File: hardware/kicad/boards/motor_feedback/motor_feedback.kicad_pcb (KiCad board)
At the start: 2 copper layers, 104 x 104 mm, 10 parts, among them J1 Screw_Terminal_01x03, J3 Screw_Terminal_01x03, U10 IL300, U11 MCP601, U9 MCP601

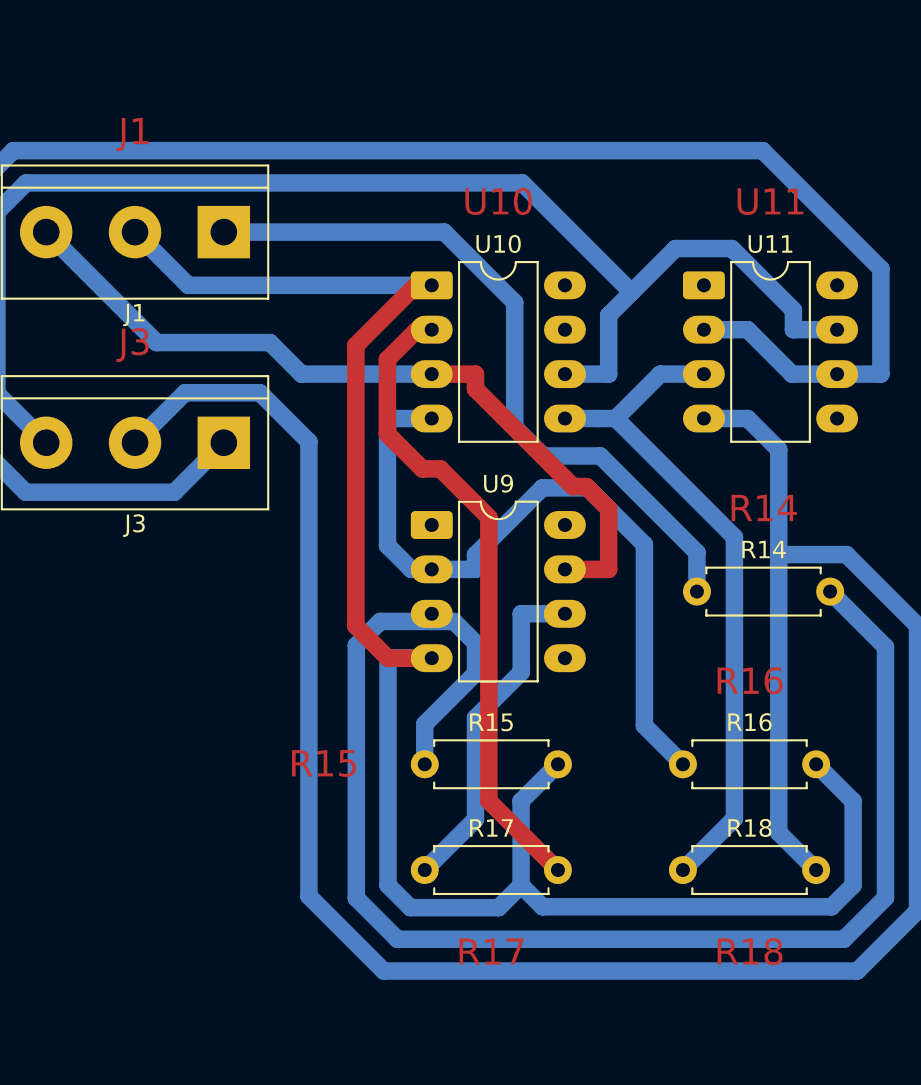
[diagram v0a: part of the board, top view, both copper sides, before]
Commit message: Refdes on silkscreen, never on top copper
Component reference designators now go on F.SilkS (top silkscreen) instead of
being etched as copper text on F.Cu. Footprint default refs are hidden so there's
one clean label per part; placement only avoids pads (silk-over-copper is fine),
so nothing drops. Also fixes the finish step's zone-removal to materialize lists
before Remove() (KiCad-10 SWIG iterators invalidate on mutation). motor_power +
motor_feedback re-finished to silk.
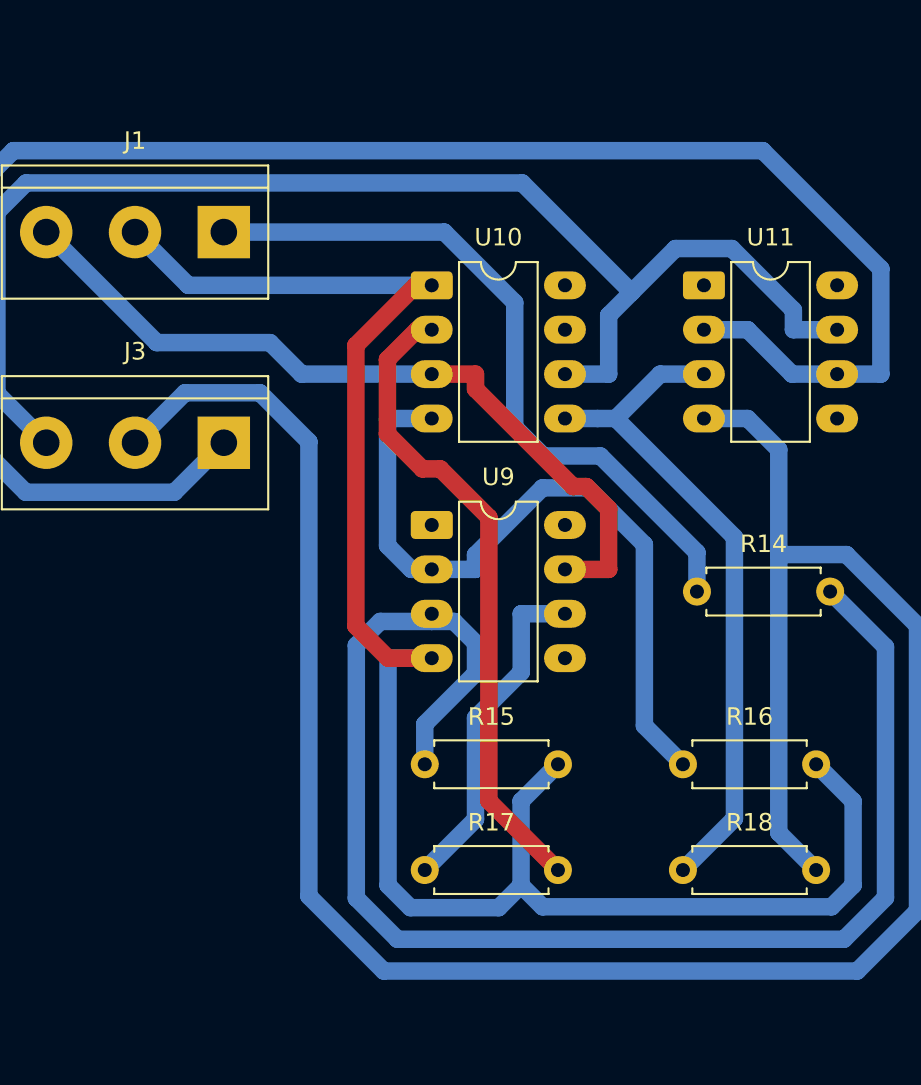
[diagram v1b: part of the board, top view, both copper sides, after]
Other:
- board text added: "U9"
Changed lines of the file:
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@@
 			(at 3.81 -2.33 0)
 			(layer "F.SilkS")
+			(hide yes)
 			(effects
 				(font
@@
 			(at 3.81 -2.33 0)
 			(layer "F.SilkS")
+			(hide yes)
 			(effects
 				(font
@@
 			(at 3.81 -2.37 0)
 			(layer "F.SilkS")
+			(hide yes)
 			(effects
 				(font
@@
 			(at 5.05 -4.65 180)
 			(layer "F.SilkS")
+			(hide yes)
 			(effects
 				(font
@@
 			(at 3.81 -2.37 0)
 			(layer "F.SilkS")
+			(hide yes)
 			(effects
 				(font
@@
 			(at 3.81 -2.37 0)
 			(layer "F.SilkS")
+			(hide yes)
 			(effects
 				(font
@@
 			(at 5.05 -4.65 180)
 			(layer "F.SilkS")
+			(hide yes)
 			(effects
 				(font
@@
 			(at 3.81 -2.33 0)
 			(layer "F.SilkS")
+			(hide yes)
 			(effects
 				(font
@@
 			(at 3.81 -2.37 0)
 			(layer "F.SilkS")
+			(hide yes)
 			(effects
 				(font
@@
 			(at 3.81 -2.37 0)
 			(layer "F.SilkS")
+			(hide yes)
 			(effects
 				(font
@@
 	)
 	(gr_text "J1"
-		(at 55.0925 49.2775 0)
-		(layer "F.Cu")
+		(at 55.0925 49.7775 0)
+		(layer "F.SilkS")
 		(effects
 			(font
-				(size 1.5 1.5)
-				(thickness 0.3)
+				(size 1 1)
+				(thickness 0.15)
 			)
 		)
 	)
 	(gr_text "J3"
-		(at 55.0925 61.3275 0)
-		(layer "F.Cu")
+		(at 55.0925 61.8275 0)
+		(layer "F.SilkS")
 		(effects
 			(font
-				(size 1.5 1.5)
-				(thickness 0.3)
+				(size 1 1)
+				(thickness 0.15)
 			)
 		)
 	)
 	(gr_text "R15"
-		(at 65.8925 85.4475 0)
-		(layer "F.Cu")
+		(at 75.4775 82.7225 0)
+		(layer "F.SilkS")
 		(effects
 			(font
-				(size 1.5 1.5)
-				(thickness 0.3)
+				(size 1 1)
+				(thickness 0.15)
 			)
 		)
 	)
 	(gr_text "R17"
-		(at 75.4775 96.2225 0)
-		(layer "F.Cu")
+		(at 75.4775 88.7725 0)
+		(layer "F.SilkS")
 		(effects
 			(font
-				(size 1.5 1.5)
-				(thickness 0.3)
+				(size 1 1)
+				(thickness 0.15)
 			)
 		)
 	)
 	(gr_text "U10"
-		(at 75.8775 53.3025 0)
-		(layer "F.Cu")
+		(at 75.8775 55.3025 0)
+		(layer "F.SilkS")
 		(effects
 			(font
-				(size 1.5 1.5)
-				(thickness 0.3)
+				(size 1 1)
+				(thickness 0.15)
+			)
+		)
+	)
+	(gr_text "U9"
+		(at 75.8775 69.0125 0)
+		(layer "F.SilkS")
+		(effects
+			(font
+				(size 1 1)
+				(thickness 0.15)
 			)
 		)
 	)
 	(gr_text "R16"
-		(at 90.2475 80.7225 0)
-		(layer "F.Cu")
+		(at 90.2475 82.7225 0)
+		(layer "F.SilkS")
 		(effects
 			(font
-				(size 1.5 1.5)
-				(thickness 0.3)
+				(size 1 1)
+				(thickness 0.15)
 			)
 		)
 	)
 	(gr_text "R18"
-		(at 90.2475 96.2225 0)
-		(layer "F.Cu")
+		(at 90.2475 88.7725 0)
+		(layer "F.SilkS")
 		(effects
 			(font
-				(size 1.5 1.5)
-				(thickness 0.3)
+				(size 1 1)
+				(thickness 0.15)
 			)
 		)
 	)
 	(gr_text "R14"
-		(at 91.0475 70.8425 0)
-		(layer "F.Cu")
+		(at 91.0475 72.8425 0)
+		(layer "F.SilkS")
 		(effects
 			(font
-				(size 1.5 1.5)
-				(thickness 0.3)
+				(size 1 1)
+				(thickness 0.15)
 			)
 		)
 	)
 	(gr_text "U11"
-		(at 91.4475 53.3025 0)
-		(layer "F.Cu")
+		(at 91.4475 55.3025 0)
+		(layer "F.SilkS")
 		(effects
 			(font
-				(size 1.5 1.5)
-				(thickness 0.3)
-			)
-		)
+				(size 1 1)
+				(thickness 0.15)
+			)
+		)
